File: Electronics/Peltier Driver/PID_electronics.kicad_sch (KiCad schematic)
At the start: 15 parts, among them J1 Conn_01x05, J2 Conn_01x03, Q3 2N7000, U1 LF412

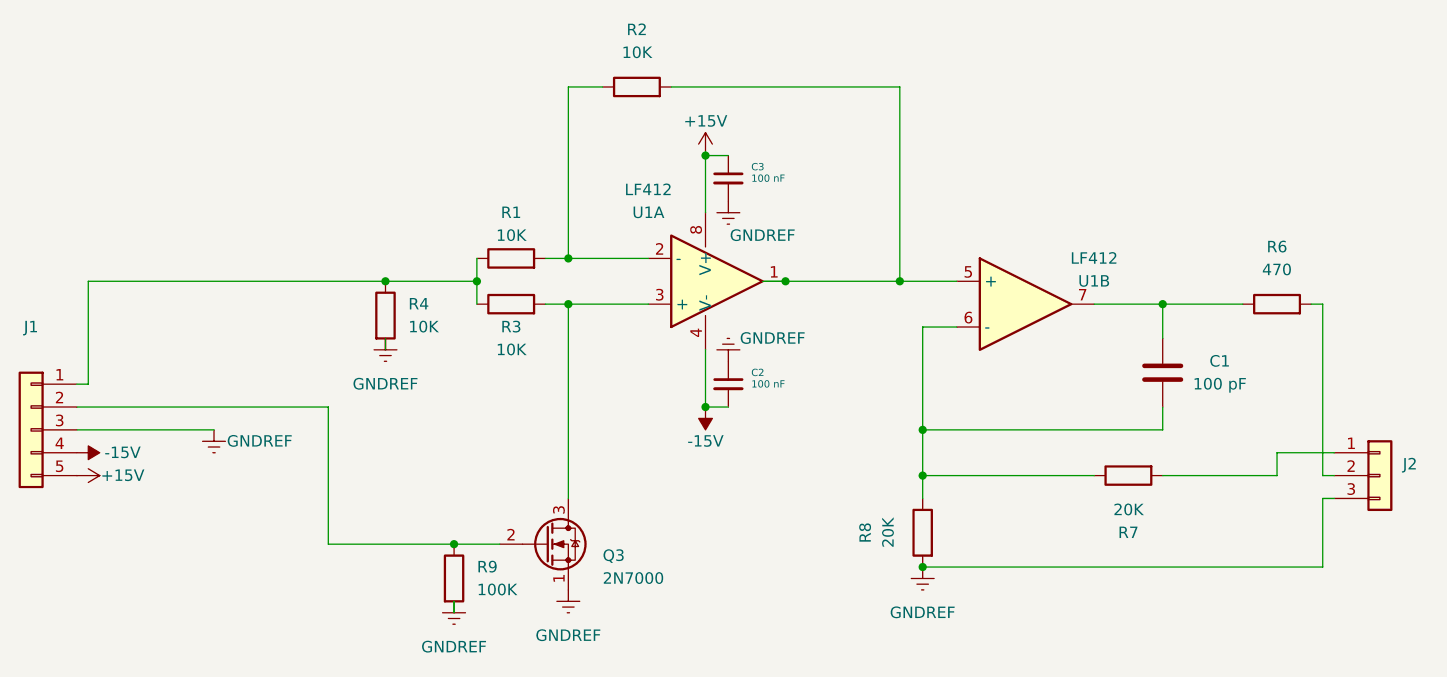
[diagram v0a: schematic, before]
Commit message: updated silkscreen
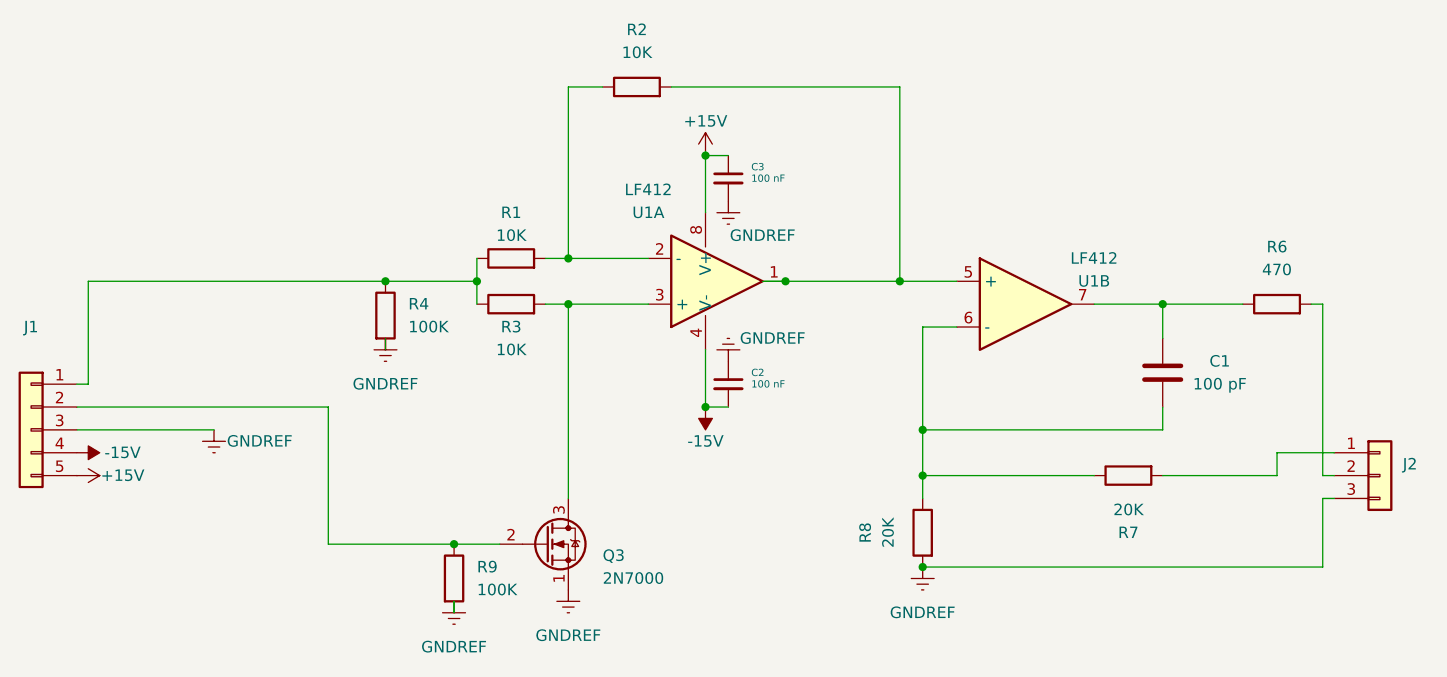
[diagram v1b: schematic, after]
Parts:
- R4: value 10K -> 100K
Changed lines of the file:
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@@
   (symbol (lib_id "power:GNDREF") (at 69.85 93.98 0) (unit 1)
     (in_bom yes) (on_board yes) (fields_autoplaced)
-    (property "Reference" "#PWR?" (id 0) (at 69.85 100.33 0)
+    (property "Reference" "#PWR0104" (id 0) (at 69.85 100.33 0)
       (effects (font (size 1.27 1.27)) hide)
     )
@@
       (effects (font (size 1.27 1.27)) (justify left))
     )
-    (property "Value" "10K" (id 1) (at 64.77 63.4999 0)
+    (property "Value" "100K" (id 1) (at 64.77 63.4999 0)
       (effects (font (size 1.27 1.27)) (justify left))
     )
@@
       (reference "#PWR0103") (unit 1) (value "GNDREF") (footprint "")
     )
+    (path "/43ee3f03-03f3-420c-96a3-8fb32d9c12c9"
+      (reference "#PWR0104") (unit 1) (value "GNDREF") (footprint "")
+    )
     (path "/a8d65b79-812a-4e13-bc6a-38fafce26ddf"
       (reference "#PWR0105") (unit 1) (value "-15V") (footprint "")
@@
       (reference "#PWR0112") (unit 1) (value "+15V") (footprint "")
     )
-    (path "/43ee3f03-03f3-420c-96a3-8fb32d9c12c9"
-      (reference "#PWR?") (unit 1) (value "GNDREF") (footprint "")
-    )
     (path "/13510096-4c4b-48f8-8107-e23cceecf7d6"
       (reference "C1") (unit 1) (value "100 pF") (footprint "Capacitor_THT:C_Axial_L3.8mm_D2.6mm_P7.50mm_Horizontal")
@@
     )
     (path "/a226fb1b-5df9-4dca-9160-13ce52ad4833"
-      (reference "R4") (unit 1) (value "10K") (footprint "Resistor_THT:R_Axial_DIN0207_L6.3mm_D2.5mm_P15.24mm_Horizontal")
+      (reference "R4") (unit 1) (value "100K") (footprint "Resistor_THT:R_Axial_DIN0207_L6.3mm_D2.5mm_P15.24mm_Horizontal")
     )
     (path "/611ccfe7-e97a-49e5-a559-7817f61cc3be"
